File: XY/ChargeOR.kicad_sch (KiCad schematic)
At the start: 5 parts, among them U1 LTC4412xS6, U3 SIRA99DP-T1-GE3

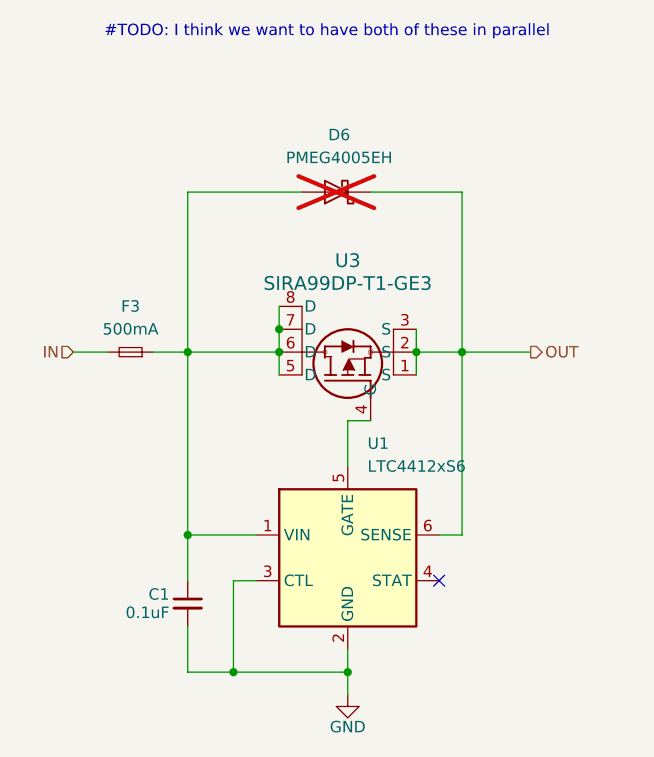
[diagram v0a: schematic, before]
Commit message: Updated layout
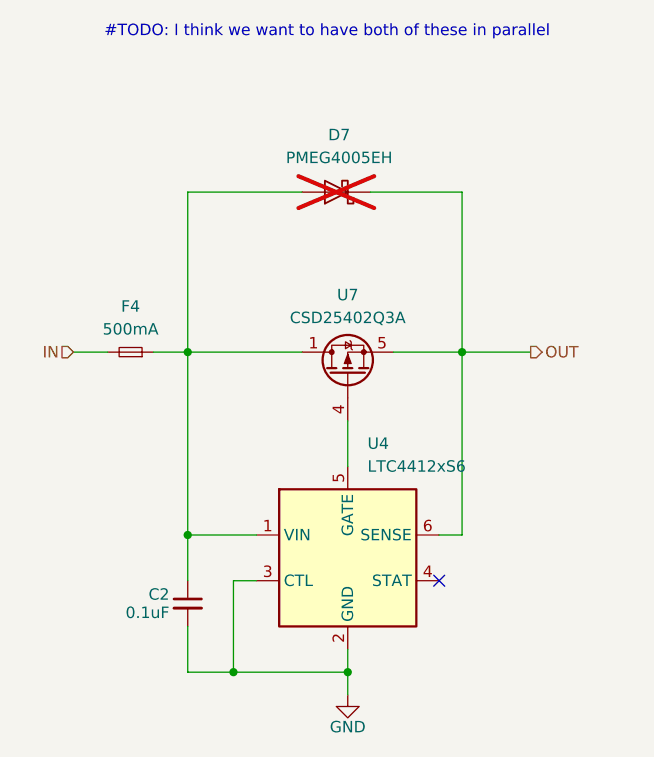
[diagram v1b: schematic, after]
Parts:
- removed U3: SIRA99DP-T1-GE3, SolarPanels:MOSFET_7DP-T1-GE3_VIS, symbol Argus-Misc:SIRA99DP-T1-GE3
- added U7: CSD25402Q3A, Package_SO:PowerPAK_SO-8_Single, symbol Transistor_FET:CSD25402Q3A
- F4: renamed from F3; footprint (none) -> Fuse:Fuse_0603_1608Metric
- renumbered C1 to C2, D6 to D7, U1 to U4
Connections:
- net OUT: now also U7.5 (S)
- net at C2.1, D7.2 (A), F4.1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: now also U7.1 (D), U7.2 (D), U7.3 (D)
- net at U4.5 (GATE): now also U7.4 (G)
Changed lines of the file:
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@@
-	)
-	(junction
-		(at 148.59 77.47)
-		(diameter 0)
-		(color 0 0 0 0)
 	)
 	(junction
@@
 		(color 0 0 0 0)
 	)
-	(junction
-		(at 133.35 77.47)
-		(diameter 0)
-		(color 0 0 0 0)
-	)
-	(junction
-		(at 133.35 74.93)
-		(diameter 0)
-		(color 0 0 0 0)
-	)
 	(no_connect
 		(at 151.13 102.87)
@@
 	(wire
 		(pts
-			(xy 148.59 74.93) (xy 148.59 77.47)
-		)
-		(stroke
-			(width 0)
-			(type default)
-		)
-	)
-	(wire
-		(pts
-			(xy 133.35 72.39) (xy 133.35 74.93)
-		)
-		(stroke
-			(width 0)
-			(type default)
-		)
-	)
-	(wire
-		(pts
 			(xy 140.97 113.03) (xy 140.97 110.49)
 		)
@@
 	(wire
 		(pts
-			(xy 140.97 85.09) (xy 143.51 85.09)
-		)
-		(stroke
-			(width 0)
-			(type default)
-		)
-	)
-	(wire
-		(pts
 			(xy 130.81 102.87) (xy 128.27 102.87)
 		)
@@
 	(wire
 		(pts
-			(xy 133.35 74.93) (xy 133.35 77.47)
-		)
-		(stroke
-			(width 0)
-			(type default)
-		)
-	)
-	(wire
-		(pts
-			(xy 123.19 77.47) (xy 133.35 77.47)
-		)
-		(stroke
-			(width 0)
-			(type default)
-		)
-	)
-	(wire
-		(pts
-			(xy 148.59 77.47) (xy 153.67 77.47)
+			(xy 123.19 77.47) (xy 135.89 77.47)
+		)
+		(stroke
+			(width 0)
+			(type default)
+		)
+	)
+	(wire
+		(pts
+			(xy 146.05 77.47) (xy 153.67 77.47)
 		)
 		(stroke
@@
 	(wire
 		(pts
-			(xy 133.35 77.47) (xy 133.35 80.01)
-		)
-		(stroke
-			(width 0)
-			(type default)
-		)
-	)
-	(wire
-		(pts
 			(xy 128.27 113.03) (xy 128.27 102.87)
 		)
@@
 		(pts
 			(xy 135.89 59.69) (xy 123.19 59.69)
-		)
-		(stroke
-			(width 0)
-			(type default)
-		)
-	)
-	(wire
-		(pts
-			(xy 148.59 77.47) (xy 148.59 80.01)
 		)
 		(stroke
@@
 		(on_board yes)
 		(dnp no)
-		(property "Reference" "C1"
+		(property "Reference" "C2"
 			(at 121.158 104.394 0)
 			(effects
@@
 		(dnp no)
 		(fields_autoplaced yes)
-		(property "Reference" "U1"
+		(property "Reference" "U4"
 			(at 143.1641 87.63 0)
 			(effects
@@
 		(dnp no)
 		(fields_autoplaced yes)
-		(property "Reference" "F3"
+		(property "Reference" "F4"
 			(at 116.84 72.39 0)
 			(effects
@@
 			)
 		)
-		(property "Footprint" ""
+		(property "Footprint" "Fuse:Fuse_0603_1608Metric"
 			(at 116.84 77.47 0)
 			(effects
@@
 				(path "/92e58b76-9357-4452-b231-18fffdf58e73/bef00a2e-eb3a-4ecf-812a-1c3ccf6e8d66/b4f3b5ea-3783-47e9-83c1-86877692286f"
 					(reference "F5")
+					(unit 1)
+				)
+			)
+		)
+	)
+	(symbol
+		(lib_id "Transistor_FET:CSD25402Q3A")
+		(at 140.97 80.01 90)
+		(unit 1)
+		(exclude_from_sim no)
+		(in_bom yes)
+		(on_board yes)
+		(dnp no)
+		(fields_autoplaced yes)
+		(property "Reference" "U7"
+			(at 140.97 71.12 90)
+			(effects
+				(font
+					(size 1.27 1.27)
+				)
+			)
+		)
+		(property "Value" "CSD25402Q3A"
+			(at 140.97 73.66 90)
+			(effects
+				(font
+					(size 1.27 1.27)
+				)
+			)
+		)
+		(property "Footprint" "Package_SO:PowerPAK_SO-8_Single"
+			(at 145.669 49.657 0)
+			(effects
+				(font
+					(size 1.27 1.27)
+				)
+				(hide yes)
+			)
+		)
+		(property "Datasheet" "https://www.ti.com/lit/ds/symlink/csd25402q3a.pdf"
+			(at 143.383 48.895 0)
+			(effects
+				(font
+					(size 1.27 1.27)
+				)
+				(hide yes)
+			)
+		)
+		(property "Description" "-76A Id, -20V Vds, NexFET P-Channel Power MOSFET, 7.7mOhm Ron, Qg (typ) 7.5 nC, VSON-8 3.3x3.3mm"
+			(at 140.97 80.01 0)
+			(effects
+				(font
+					(size 1.27 1.27)
+				)
+				(hide yes)
+			)
+		)
+		(pin "3"
+		)
+		(pin "1"
+		)
+		(pin "5"
+		)
+		(pin "2"
+		)
+		(pin "4"
+		)
+		(instances
+			(project ""
+				(path "/92e58b76-9357-4452-b231-18fffdf58e73/bef00a2e-eb3a-4ecf-812a-1c3ccf6e8d66/16f90485-8271-472f-a87a-9c27ffab6e8f"
+					(reference "U7")
+					(unit 1)
+				)
+				(path "/92e58b76-9357-4452-b231-18fffdf58e73/bef00a2e-eb3a-4ecf-812a-1c3ccf6e8d66/6c74510c-fc2f-4690-9a5b-9f1baf296eee"
+					(reference "U3")
+					(unit 1)
+				)
+				(path "/92e58b76-9357-4452-b231-18fffdf58e73/bef00a2e-eb3a-4ecf-812a-1c3ccf6e8d66/b4f3b5ea-3783-47e9-83c1-86877692286f"
+					(reference "U9")
 					(unit 1)
 				)
@@
 		(on_board yes)
 		(dnp no)
-		(property "Reference" "#PWR01"
+		(property "Reference" "#PWR02"
 			(at 140.97 121.92 0)
 			(effects
@@
 				(path "/92e58b76-9357-4452-b231-18fffdf58e73/bef00a2e-eb3a-4ecf-812a-1c3ccf6e8d66/b4f3b5ea-3783-47e9-83c1-86877692286f"
 					(reference "#PWR03")
-					(unit 1)
-				)
-			)
-		)
-	)
-	(symbol
-		(lib_id "Argus-Misc:SIRA99DP-T1-GE3")
-		(at 143.51 85.09 270)
-		(mirror x)
-		(unit 1)
-		(exclude_from_sim no)
-		(in_bom yes)
-		(on_board yes)
-		(dnp no)
-		(fields_autoplaced yes)
-		(property "Reference" "U3"
-			(at 140.97 67.31 90)
-			(effects
-				(font
-					(size 1.524 1.524)
-				)
-			)
-		)
-		(property "Value" "SIRA99DP-T1-GE3"
-			(at 140.97 69.85 90)
-			(effects
-				(font
-					(size 1.524 1.524)
-				)
-			)
-		)
-		(property "Footprint" "SolarPanels:MOSFET_7DP-T1-GE3_VIS"
-			(at 143.51 85.09 0)
-			(effects
-				(font
-					(size 1.27 1.27)
-					(italic yes)
-				)
-				(hide yes)
-			)
-		)
-		(property "Datasheet" "SIRA99DP-T1-GE3"
-			(at 143.51 85.09 0)
-			(effects
-				(font
-					(size 1.27 1.27)
-					(italic yes)
-				)
-				(hide yes)
-			)
-		)
-		(property "Description" ""
-			(at 143.51 85.09 0)
-			(effects
-				(font
-					(size 1.27 1.27)
-				)
-				(hide yes)
-			)
-		)
-		(pin "5"
-		)
-		(pin "6"
-		)
-		(pin "7"
-		)
-		(pin "8"
-		)
-		(pin "2"
-		)
-		(pin "1"
-		)
-		(pin "4"
-		)
-		(pin "3"
-		)
-		(instances
-			(project "Avionics-SolarPanels"
-				(path "/92e58b76-9357-4452-b231-18fffdf58e73/bef00a2e-eb3a-4ecf-812a-1c3ccf6e8d66/16f90485-8271-472f-a87a-9c27ffab6e8f"
-					(reference "U7")
-					(unit 1)
-				)
-				(path "/92e58b76-9357-4452-b231-18fffdf58e73/bef00a2e-eb3a-4ecf-812a-1c3ccf6e8d66/6c74510c-fc2f-4690-9a5b-9f1baf296eee"
-					(reference "U3")
-					(unit 1)
-				)
-				(path "/92e58b76-9357-4452-b231-18fffdf58e73/bef00a2e-eb3a-4ecf-812a-1c3ccf6e8d66/b4f3b5ea-3783-47e9-83c1-86877692286f"
-					(reference "U9")
 					(unit 1)
 				)
@@
 		(dnp yes)
 		(fields_autoplaced yes)
-		(property "Reference" "D6"
+		(property "Reference" "D7"
 			(at 140.0175 53.34 0)
 			(effects

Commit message: Updated 3d models, footprints
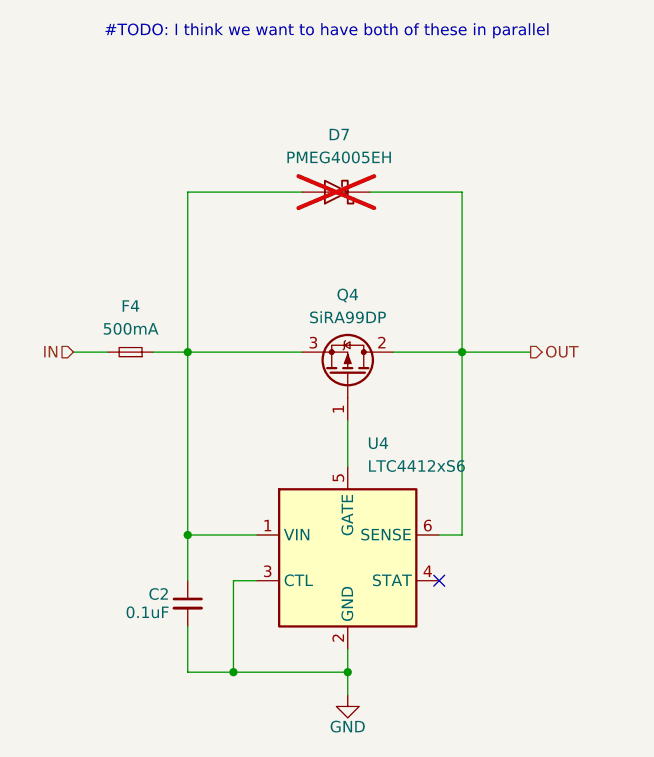
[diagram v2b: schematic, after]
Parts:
- removed U7: CSD25402Q3A, Package_SO:PowerPAK_SO-8_Single, symbol Transistor_FET:CSD25402Q3A
- added Q4: SiRA99DP, Argus-Miscellaneous:PowerPAK SO-8, symbol Argus-IC:Q_PMOS_GDS
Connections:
- net OUT: now also Q4.2 (D)
- net at C2.1, D7.2 (A), F4.1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: now also Q4.3 (S)
- net at U4.5 (GATE): now also Q4.1 (G)
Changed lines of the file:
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@@
 	)
 	(symbol
-		(lib_id "Transistor_FET:CSD25402Q3A")
-		(at 140.97 80.01 90)
+		(lib_id "Argus-IC:Q_PMOS_GDS")
+		(at 140.97 80.01 270)
+		(mirror x)
 		(unit 1)
 		(exclude_from_sim no)
@@
 		(on_board yes)
 		(dnp no)
-		(fields_autoplaced yes)
-		(property "Reference" "U7"
+		(property "Reference" "Q4"
 			(at 140.97 71.12 90)
 			(effects
@@
 			)
 		)
-		(property "Value" "CSD25402Q3A"
+		(property "Value" "SiRA99DP"
 			(at 140.97 73.66 90)
 			(effects
@@
 			)
 		)
-		(property "Footprint" "Package_SO:PowerPAK_SO-8_Single"
-			(at 145.669 49.657 0)
+		(property "Footprint" "Argus-Miscellaneous:PowerPAK SO-8"
+			(at 143.51 74.93 0)
 			(effects
 				(font
@@
 			)
 		)
-		(property "Datasheet" "https://www.ti.com/lit/ds/symlink/csd25402q3a.pdf"
-			(at 143.383 48.895 0)
+		(property "Datasheet" "~"
+			(at 140.97 80.01 0)
 			(effects
 				(font
@@
 			)
 		)
-		(property "Description" "-76A Id, -20V Vds, NexFET P-Channel Power MOSFET, 7.7mOhm Ron, Qg (typ) 7.5 nC, VSON-8 3.3x3.3mm"
+		(property "Description" "P-MOSFET transistor, gate/drain/source"
 			(at 140.97 80.01 0)
 			(effects
@@
 		(pin "3"
 		)
-		(pin "1"
-		)
-		(pin "5"
-		)
 		(pin "2"
 		)
-		(pin "4"
+		(pin "1"
 		)
 		(instances
 			(project ""
 				(path "/92e58b76-9357-4452-b231-18fffdf58e73/bef00a2e-eb3a-4ecf-812a-1c3ccf6e8d66/16f90485-8271-472f-a87a-9c27ffab6e8f"
-					(reference "U7")
+					(reference "Q4")
 					(unit 1)
 				)
 				(path "/92e58b76-9357-4452-b231-18fffdf58e73/bef00a2e-eb3a-4ecf-812a-1c3ccf6e8d66/6c74510c-fc2f-4690-9a5b-9f1baf296eee"
-					(reference "U3")
+					(reference "Q3")
 					(unit 1)
 				)
 				(path "/92e58b76-9357-4452-b231-18fffdf58e73/bef00a2e-eb3a-4ecf-812a-1c3ccf6e8d66/b4f3b5ea-3783-47e9-83c1-86877692286f"
-					(reference "U9")
+					(reference "Q5")
 					(unit 1)
 				)
